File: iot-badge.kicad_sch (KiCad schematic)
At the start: 28 parts, among them J1 USB_C_Receptacle_USB2.0, Q1 BC847, Q2 BC847, SW1 SW_Push, SW2 SW_Push, SW3 SW_Push, SW4 SW_Push, SW5 SW_Push, SW6 SW_Push, U1 ESP32-WROOM-32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

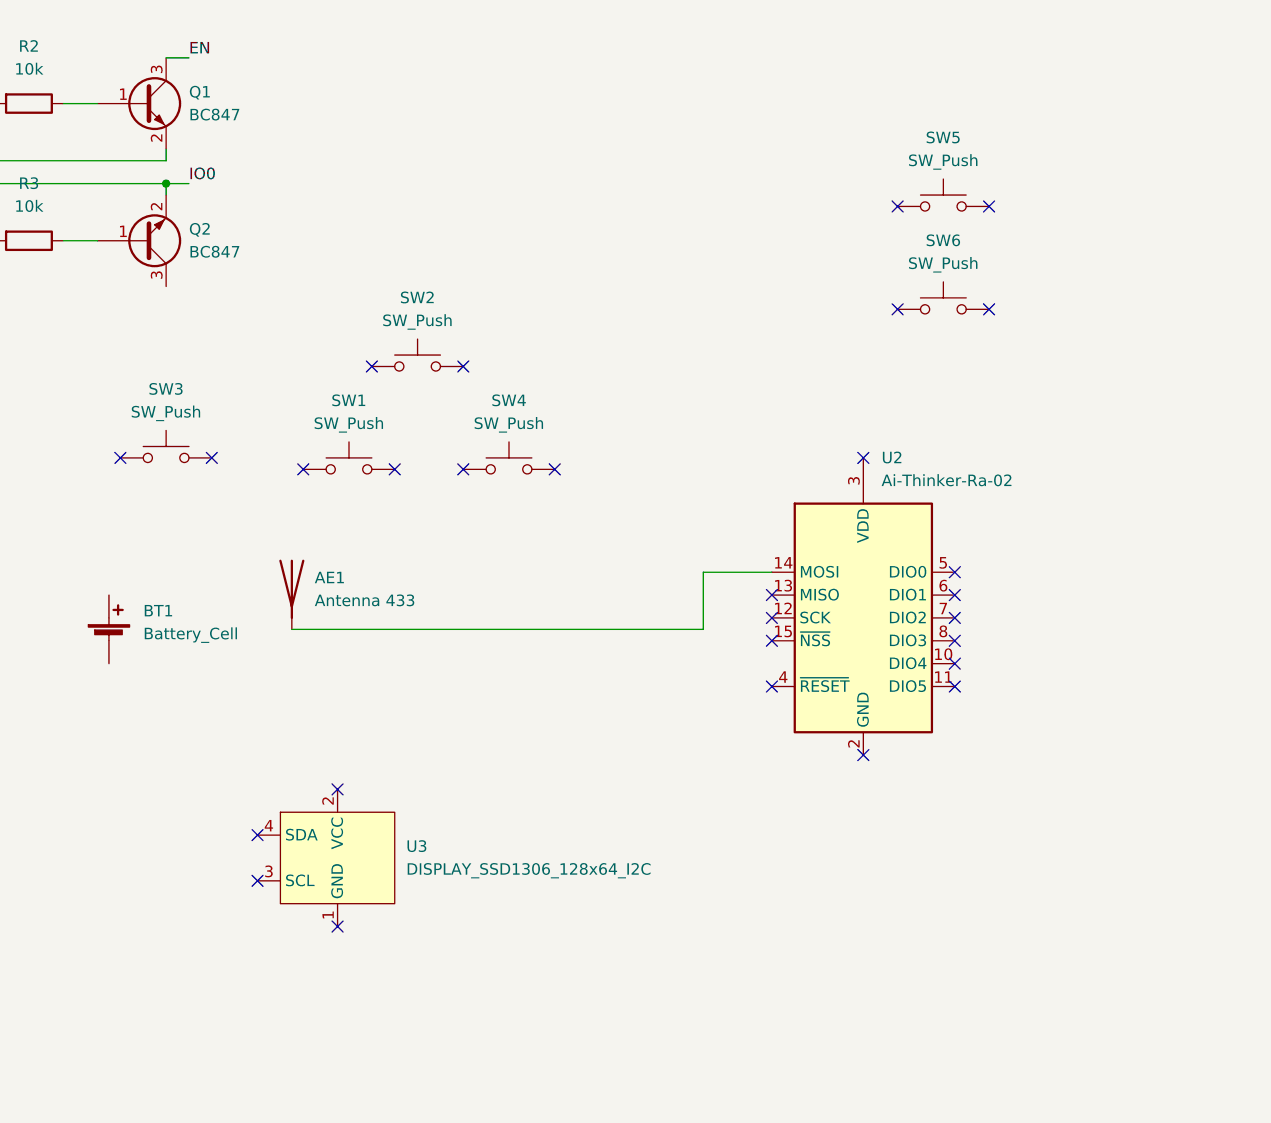
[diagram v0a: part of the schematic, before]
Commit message: pcb ant fixed
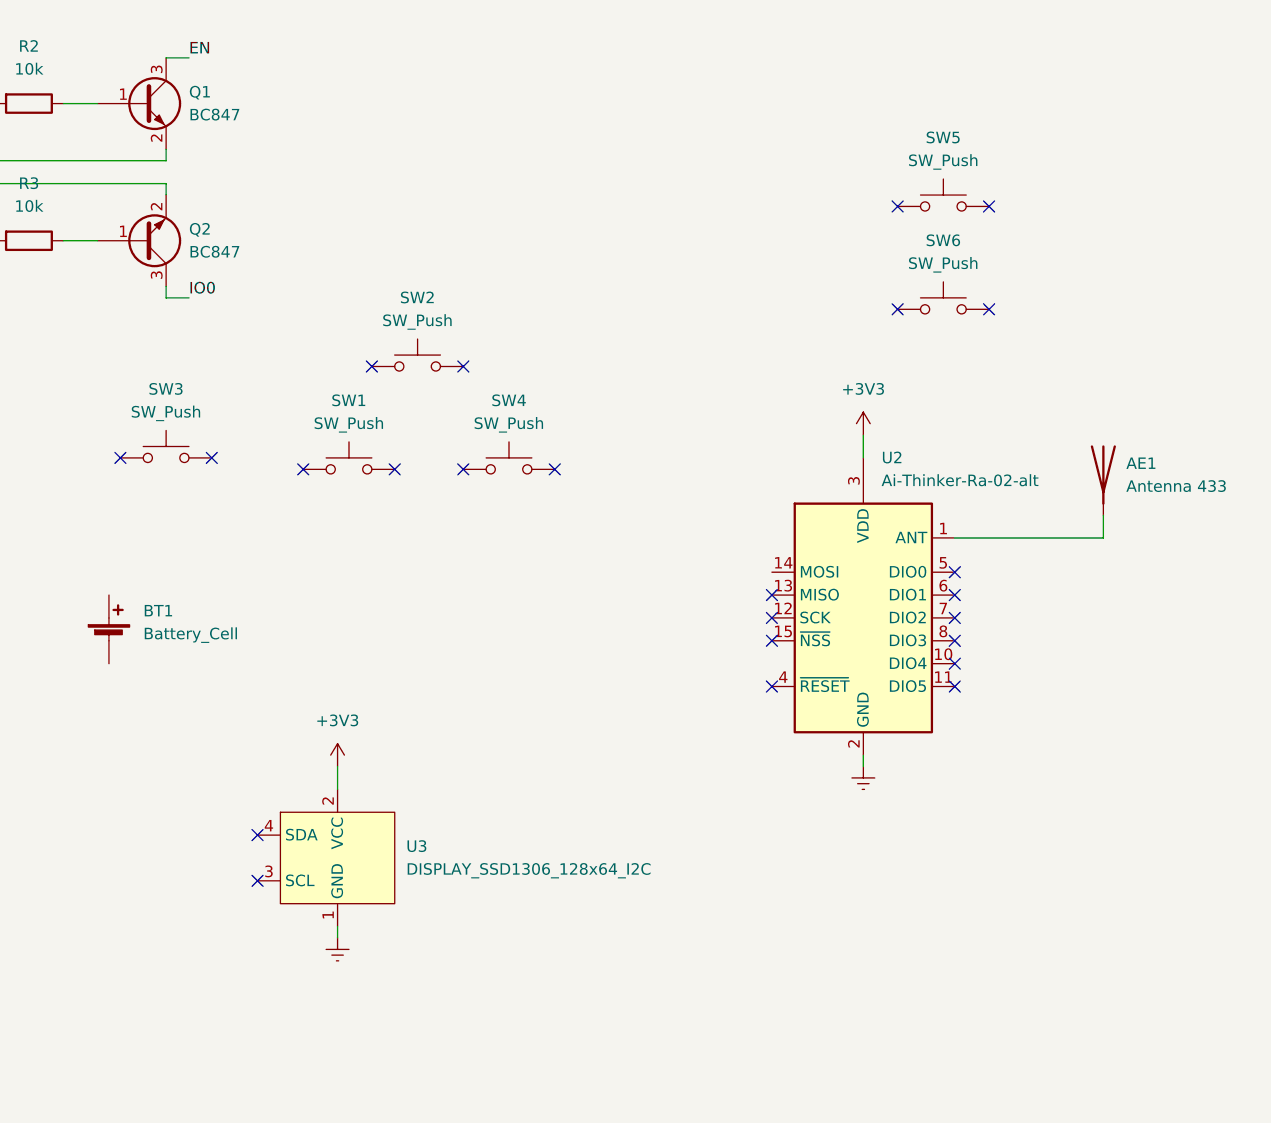
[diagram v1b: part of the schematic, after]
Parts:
- removed U2: Ai-Thinker-Ra-02, RF_Module:Ai-Thinker-Ra-01-LoRa, symbol RF_Module:Ai-Thinker-Ra-02
- added U2: Ai-Thinker-Ra-02-alt, RF_Module_alt:Ai-Thinker-Ra-02-LoRa-alt, symbol RF_Module_alt:Ai-Thinker-Ra-02-alt
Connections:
- net +3V3: now also U3.2 (VCC), U2.3 (VDD)
- net Earth: now also U3.1 (GND), U2.16 (GND), U2.2 (GND), U2.9 (GND)
- net IO0: now also Q2.3 (C); no longer Q2.2 (E), R2.2, U5.13 (~{DTR})
- net at AE1.1 (A): now also U2.1 (ANT)
- new net: Q2.2 (E), R2.2, U5.13 (~{DTR})
- no-connect marks 67 -> 63
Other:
- moved on the sheet: AE1

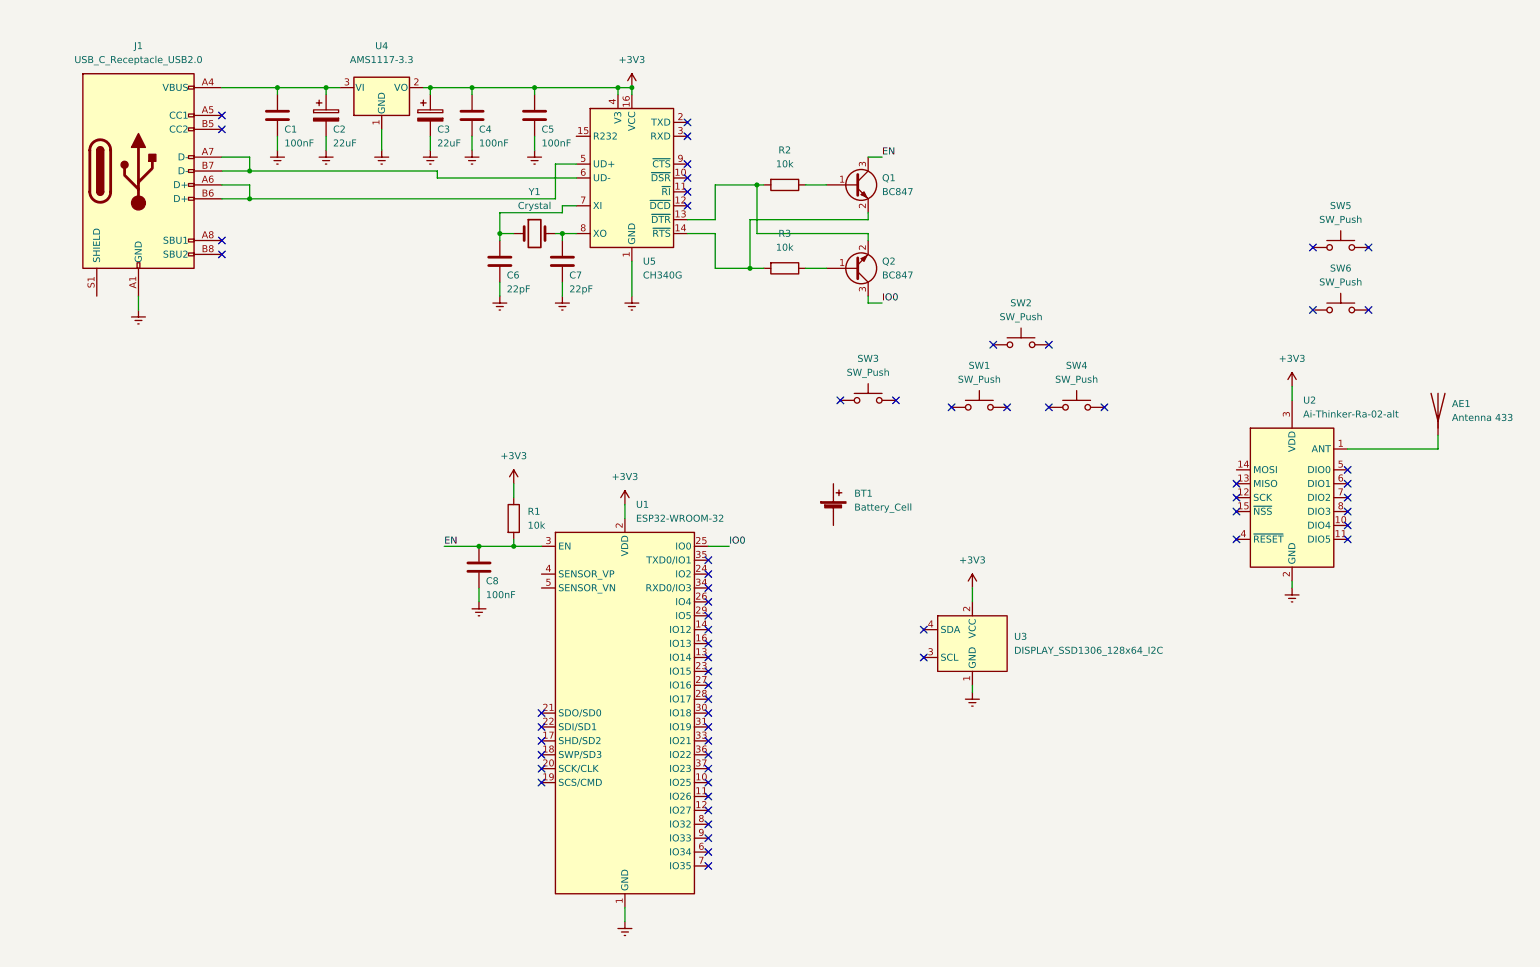
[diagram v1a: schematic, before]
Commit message: connected lora and screen
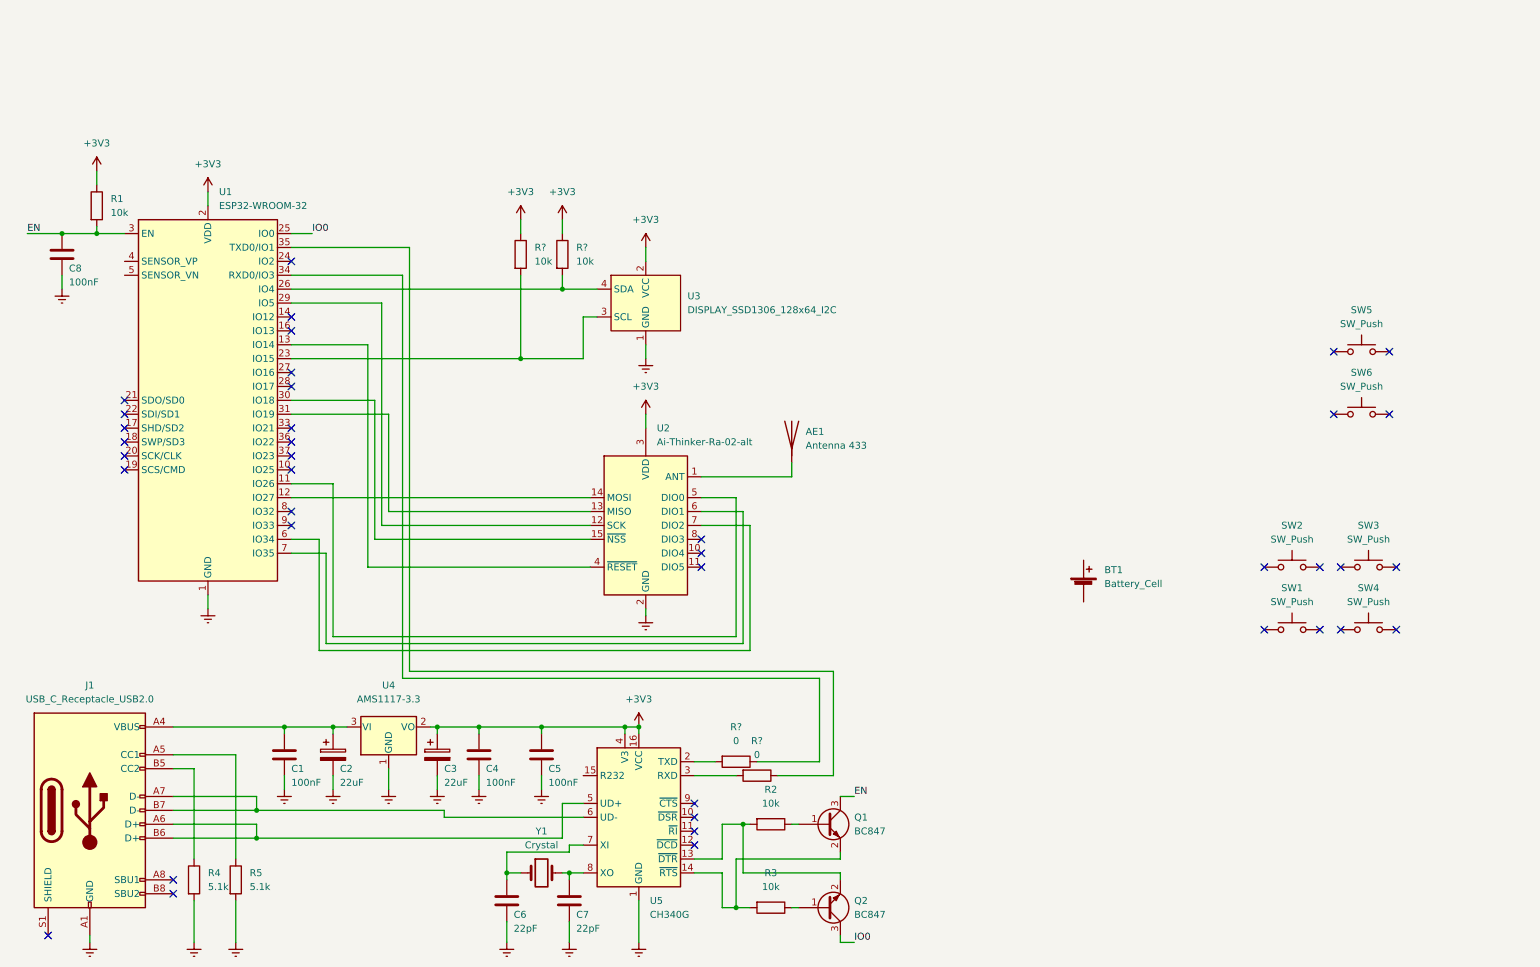
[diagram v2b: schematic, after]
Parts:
- added R4, R5: 5.1k, Resistor_SMD:R_0805_2012Metric_Pad1.20x1.40mm_HandSolder, symbol Device:R
- added R? (x2): 10k, Resistor_SMD:R_0805_2012Metric_Pad1.20x1.40mm_HandSolder, symbol Device:R
- added R? (x2): 0, Resistor_SMD:R_0805_2012Metric_Pad1.20x1.40mm_HandSolder, symbol Device:R
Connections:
- net +3V3: now also R?.1, R?.1
- net Earth: now also R4.2, R5.2
- net at U5.2 (TXD): now also R?.2
- net at U5.3 (RXD): now also R?.2
- net at U2.12 (SCK): now also U1.29 (IO5)
- net at U2.13 (MISO): now also U1.31 (IO19)
- net at U2.14 (MOSI): now also U1.12 (IO27)
- net at U2.15 (~{NSS}): now also U1.30 (IO18)
- net at U2.4 (~{RESET}): now also U1.13 (IO14)
- net at U2.5 (DIO0): now also U1.11 (IO26)
- net at U2.6 (DIO1): now also U1.7 (IO35)
- net at U2.7 (DIO2): now also U1.6 (IO34)
- net at J1.A5 (CC1): now also R5.1
- net at J1.B5 (CC2): now also R4.1
- net at U3.3 (SCL): now also U1.23 (IO15), R?.2
- net at U3.4 (SDA): now also U1.26 (IO4), R?.2
- net at U1.34 (RXD0/IO3): now also R?.1
- net at U1.35 (TXD0/IO1): now also R?.1
- no-connect marks 63 -> 39
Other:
- moved on the sheet: AE1, BT1, C1, C2, C3, C4, C5, C6, C7, C8, J1, Q1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

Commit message: added res buttons and almost routable
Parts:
- added SW7: E, Button_Switch_SMD:SW_Push_SPST_NO_Alps_SKRK, symbol Switch:SW_Push
- added SW8: 0, Button_Switch_SMD:SW_Push_SPST_NO_Alps_SKRK, symbol Switch:SW_Push
- gave numbers to parts that had none: 4
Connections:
- net EN: now also SW7.2
- net Earth: now also SW7.1, SW8.2
- net IO0: now also SW8.1
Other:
- moved on the sheet: C8

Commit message: added crystal and led rgb
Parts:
- added D1: LED_RGB, LED_SMD:LED_RGB_5050-6, symbol Device:LED_RGB
- Y1: footprint Crystal:Crystal_SMD_0603-2Pin_6.0x3.5mm_HandSoldering -> Crystal:Crystal_SMD_HC49-SD_HandSoldering
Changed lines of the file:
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@@
     (pin "2")
+  )
+  (symbol (lib_id "Device:LED_RGB") (at 222.25 88.9 0) (unit 1)
+    (in_bom yes) (on_board yes) (fields_autoplaced)
+    (property "Reference" "D1" (id 0) (at 222.25 74.93 0))
+    (property "Value" "LED_RGB" (id 1) (at 222.25 77.47 0))
+    (property "Footprint" "LED_SMD:LED_RGB_5050-6" (id 2) (at 222.25 90.17 0)
+      (effects (font (size 1.27 1.27)) hide)
+    )
+    (property "Datasheet" "~" (id 3) (at 222.25 90.17 0)
+      (effects (font (size 1.27 1.27)) hide)
+    )
+    (pin "1")
+    (pin "2")
+    (pin "3")
+    (pin "4")
+    (pin "5")
+    (pin "6")
   )
   (symbol (lib_id "power:+3V3") (at 128.27 149.86 0) (unit 1)
@@
     (property "Reference" "Y1" (id 0) (at 110.49 168.91 0))
     (property "Value" "Crystal" (id 1) (at 110.49 171.45 0))
-    (property "Footprint" "Crystal:Crystal_SMD_0603-2Pin_6.0x3.5mm_HandSoldering" (id 2) (at 110.49 176.53 0)
+    (property "Footprint" "Crystal:Crystal_SMD_HC49-SD_HandSoldering" (id 2) (at 110.49 176.53 0)
       (effects (font (size 1.27 1.27)) hide)
     )
@@
       (reference "C8") (unit 1) (value "100nF") (footprint "Capacitor_SMD:C_0805_2012Metric_Pad1.18x1.45mm_HandSolder")
     )
+    (path "/2dbc282c-a4c9-44f2-b1b6-9acbf2576b02"
+      (reference "D1") (unit 1) (value "LED_RGB") (footprint "LED_SMD:LED_RGB_5050-6")
+    )
     (path "/b1b227c3-763e-438d-aed7-d3f1dd332c2c"
       (reference "J1") (unit 1) (value "USB_C_Receptacle_USB2.0") (footprint "Connector_USB:USB_C_Receptacle_HRO_TYPE-C-31-M-12")
@@
     )
     (path "/b6bf3229-edbf-4e20-84e4-316f6abc0502"
-      (reference "Y1") (unit 1) (value "Crystal") (footprint "Crystal:Crystal_SMD_0603-2Pin_6.0x3.5mm_HandSoldering")
-    )
-  )
+      (reference "Y1") (unit 1) (value "Crystal") (footprint "Crystal:Crystal_SMD_HC49-SD_HandSoldering")
+    )
+  )

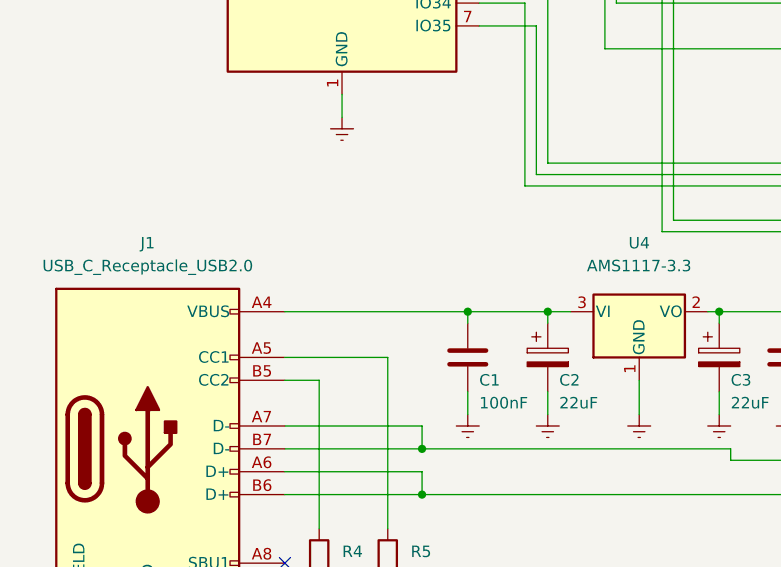
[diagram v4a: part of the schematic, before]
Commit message: diode added to power
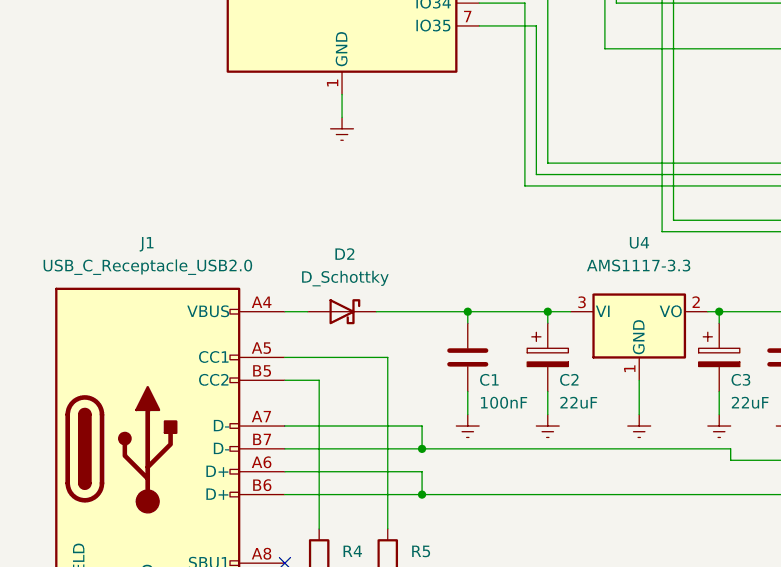
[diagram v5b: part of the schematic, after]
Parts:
- added D2: D_Schottky, Diode_SMD:D_SOD-123, symbol Device:D_Schottky
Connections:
- net at J1.A4 (VBUS), J1.A9 (VBUS), J1.B4 (VBUS)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: now also D2.2 (A); no longer C1.1, C2.1, U4.3 (VI)
- new net: C1.1, C2.1, D2.1 (K), U4.3 (VI)
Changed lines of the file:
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@@
   (junction (at 29.21 59.69) (diameter 0) (color 0 0 0 0)
   )
+  (junction (at 21.59 59.69) (diameter 0) (color 0 0 0 0)
+  )
+  (junction (at 99.06 149.86) (diameter 0) (color 0 0 0 0)
+  )
+  (junction (at 128.27 149.86) (diameter 0) (color 0 0 0 0)
+  )
+  (junction (at 125.73 149.86) (diameter 0) (color 0 0 0 0)
+  )
+  (junction (at 58.42 170.18) (diameter 0) (color 0 0 0 0)
+  )
+  (junction (at 26.67 71.12) (diameter 0) (color 0 0 0 0)
+  )
+  (junction (at 26.67 59.69) (diameter 0) (color 0 0 0 0)
+  )
+  (junction (at 72.39 149.86) (diameter 0) (color 0 0 0 0)
+  )
+  (junction (at 91.44 149.86) (diameter 0) (color 0 0 0 0)
+  )
   (junction (at 63.5 149.86) (diameter 0) (color 0 0 0 0)
-  )
-  (junction (at 21.59 59.69) (diameter 0) (color 0 0 0 0)
-  )
-  (junction (at 99.06 149.86) (diameter 0) (color 0 0 0 0)
-  )
-  (junction (at 128.27 149.86) (diameter 0) (color 0 0 0 0)
-  )
-  (junction (at 125.73 149.86) (diameter 0) (color 0 0 0 0)
-  )
-  (junction (at 58.42 170.18) (diameter 0) (color 0 0 0 0)
-  )
-  (junction (at 26.67 71.12) (diameter 0) (color 0 0 0 0)
-  )
-  (junction (at 26.67 59.69) (diameter 0) (color 0 0 0 0)
-  )
-  (junction (at 72.39 149.86) (diameter 0) (color 0 0 0 0)
-  )
-  (junction (at 91.44 149.86) (diameter 0) (color 0 0 0 0)
   )
   (junction (at 110.49 149.86) (diameter 0) (color 0 0 0 0)
@@
     (stroke (width 0) (type default) (color 0 0 0 0))
   )
+  (wire (pts (xy 43.18 149.86) (xy 45.72 149.86))
+    (stroke (width 0) (type default) (color 0 0 0 0))
+  )
   (wire (pts (xy 99.06 158.75) (xy 99.06 161.29))
     (stroke (width 0) (type default) (color 0 0 0 0))
@@
     (stroke (width 0) (type default) (color 0 0 0 0))
   )
-  (wire (pts (xy 43.18 149.86) (xy 63.5 149.86))
-    (stroke (width 0) (type default) (color 0 0 0 0))
-  )
   (wire (pts (xy 64.77 59.69) (xy 67.31 59.69))
     (stroke (width 0) (type default) (color 0 0 0 0))
@@
   )
   (wire (pts (xy 106.68 82.55) (xy 118.11 82.55))
+    (stroke (width 0) (type default) (color 0 0 0 0))
+  )
+  (wire (pts (xy 53.34 149.86) (xy 63.5 149.86))
     (stroke (width 0) (type default) (color 0 0 0 0))
   )
@@
     )
     (property "Datasheet" "~" (id 3) (at 146.05 156.21 0)
+      (effects (font (size 1.27 1.27)) hide)
+    )
+    (pin "1")
+    (pin "2")
+  )
+  (symbol (lib_id "Device:D_Schottky") (at 49.53 149.86 0) (mirror y) (unit 1)
+    (in_bom yes) (on_board yes) (fields_autoplaced)
+    (property "Reference" "D2" (id 0) (at 49.8475 143.51 0))
+    (property "Value" "D_Schottky" (id 1) (at 49.8475 146.05 0))
+    (property "Footprint" "Diode_SMD:D_SOD-123" (id 2) (at 49.53 149.86 0)
+      (effects (font (size 1.27 1.27)) hide)
+    )
+    (property "Datasheet" "~" (id 3) (at 49.53 149.86 0)
       (effects (font (size 1.27 1.27)) hide)
     )
@@
       (reference "D1") (unit 1) (value "LED_RGB") (footprint "LED_SMD:LED_RGB_5050-6")
     )
+    (path "/bbb63548-4b1d-4129-bec8-c19b9405207d"
+      (reference "D2") (unit 1) (value "D_Schottky") (footprint "Diode_SMD:D_SOD-123")
+    )
     (path "/b1b227c3-763e-438d-aed7-d3f1dd332c2c"
